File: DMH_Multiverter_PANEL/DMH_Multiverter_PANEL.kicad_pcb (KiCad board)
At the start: 2 copper layers, 50 x 200 mm, 5 parts, among them J0 Panel_GND_Solder_Wire_Pad

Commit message: Panel ready
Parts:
- added H10: Attenuate, SynthStuff:Pot_Cutout_Small_attv, F.Cu at (83.0, 97.0)
- added H11: Input, SynthStuff:Jack_6.35mm_Cutout_v3, F.Cu at (58.5, 126.2)
- added H12: Output, SynthStuff:Jack_6.35mm_Cutout_Output_v6, F.Cu at (75.0, 126.2)
- added H13: Output, SynthStuff:Jack_6.35mm_Cutout_Output_v6, F.Cu at (91.5, 126.2)
- added H14: Input, SynthStuff:Jack_6.35mm_Cutout_v3, F.Cu at (58.5, 142.8)
- added H15: Output, SynthStuff:Jack_6.35mm_Cutout_Output_v6, F.Cu at (75.0, 142.8)
- added H16: Output, SynthStuff:Jack_6.35mm_Cutout_Output_v6, F.Cu at (91.5, 142.8)
- added H17: Input, SynthStuff:Jack_6.35mm_Cutout_v3, F.Cu at (58.5, 159.2)
- added H18: Output, SynthStuff:Jack_6.35mm_Cutout_Output_v6, F.Cu at (75.0, 159.2)
- added H19: Output, SynthStuff:Jack_6.35mm_Cutout_Output_v6, F.Cu at (91.5, 159.2)
- added H20: Input, SynthStuff:Jack_6.35mm_Cutout_v3, F.Cu at (58.5, 175.8)
- added H21: Output, SynthStuff:Jack_6.35mm_Cutout_Output_v6, F.Cu at (75.0, 175.8)
- added H22: Output, SynthStuff:Jack_6.35mm_Cutout_Output_v6, F.Cu at (91.5, 175.8)
- added H23: Input, SynthStuff:Jack_6.35mm_Cutout_v3, F.Cu at (58.5, 192.2)
- added H24: Output, SynthStuff:Jack_6.35mm_Cutout_Output_v6, F.Cu at (75.0, 192.2)
- added H25: Output, SynthStuff:Jack_6.35mm_Cutout_Output_v6, F.Cu at (91.5, 192.2)
- added H26: Input, SynthStuff:Jack_6.35mm_Cutout_v3, F.Cu at (58.5, 208.8)
- added H27: Output, SynthStuff:Jack_6.35mm_Cutout_Output_v6, F.Cu at (75.0, 208.8)
- added H28: Output, SynthStuff:Jack_6.35mm_Cutout_Output_v6, F.Cu at (91.5, 208.8)
- added H5: Input, SynthStuff:Jack_6.35mm_Cutout_v3, F.Cu at (58.5, 50.0)
- added H6: Output, SynthStuff:Jack_6.35mm_Cutout_Output_v6, F.Cu at (58.5, 67.0)
- added H7: Attenuate, SynthStuff:Pot_Cutout_Small_attv, F.Cu at (83.0, 58.8)
- added H8: Input, SynthStuff:Jack_6.35mm_Cutout_v3, F.Cu at (58.5, 88.2)
- added H9: Output, SynthStuff:Jack_6.35mm_Cutout_Output_v6, F.Cu at (58.5, 105.2)
- moved J0 65.6 mm to (95.0, 78.0)
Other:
- board text added: "Attn & Mult"
- board text removed: "Module Name"
- board text removed: "TYPE"

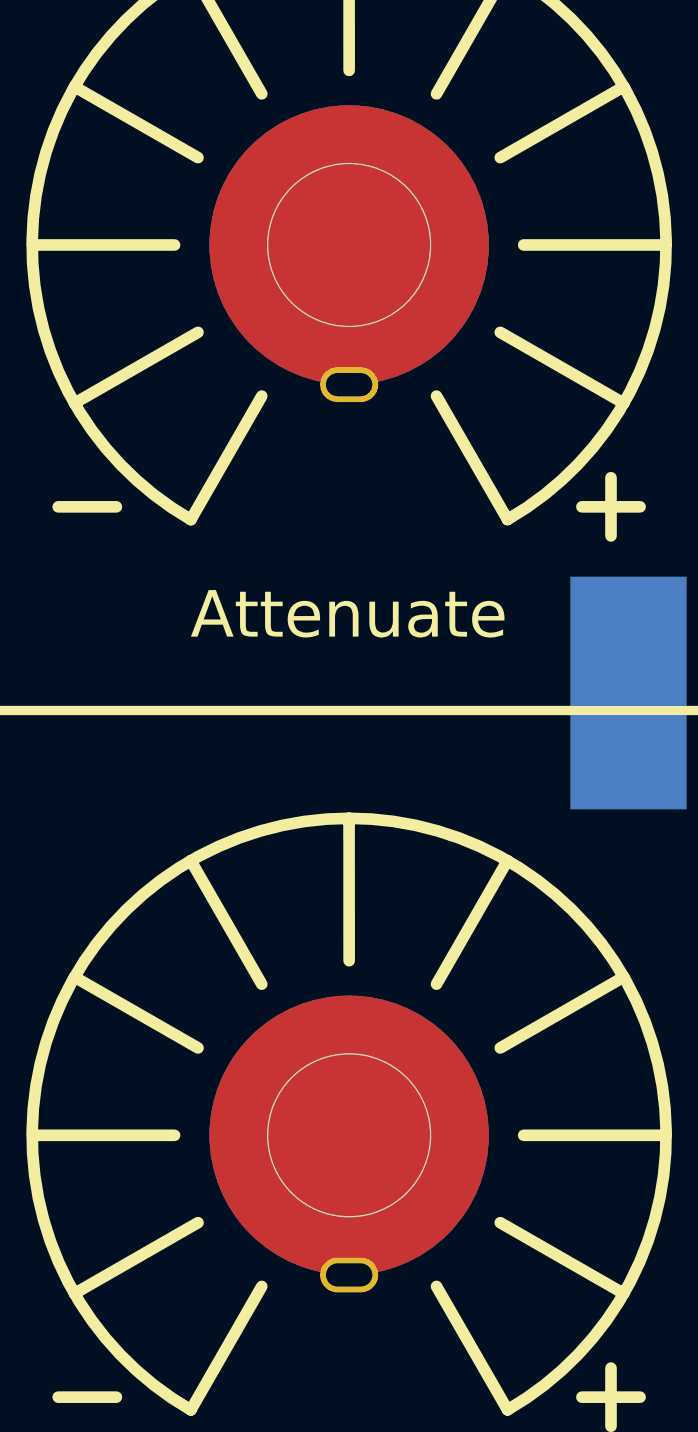
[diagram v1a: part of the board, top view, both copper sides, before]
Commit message: Adapted design to center detent pot P110KH-1F15
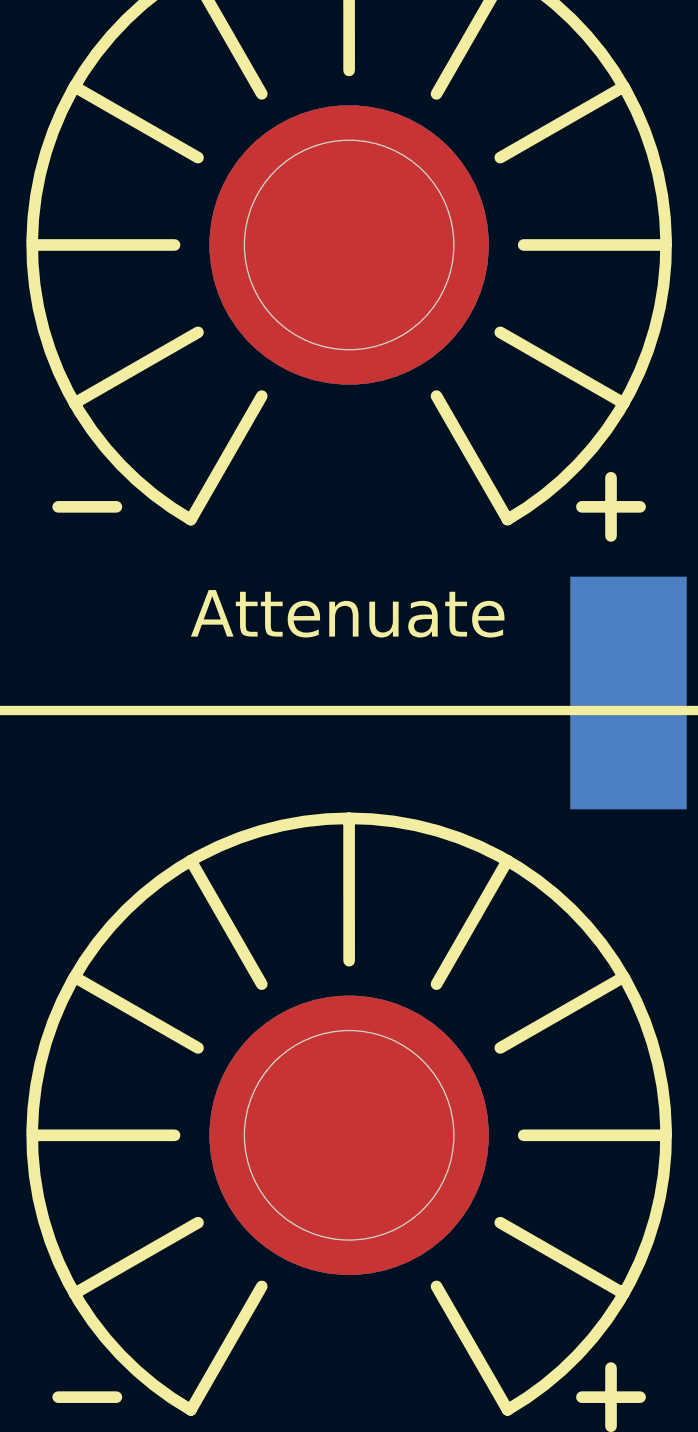
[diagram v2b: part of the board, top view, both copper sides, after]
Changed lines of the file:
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@@
 		(fp_circle
 			(center 0 0)
-			(end 0 3.5)
+			(end 4.5 0)
 			(stroke
 				(width 0.05)
@@
 			(size 12 12)
 			(layers "B.Cu" "B.Mask")
-			(net 1 "GND")
-			(pinfunction "1")
-			(pintype "input")
-			(zone_connect 2)
-		)
-		(pad "1" thru_hole oval
-			(at 0 6)
-			(size 2.5 1.5)
-			(drill oval 2 1)
-			(layers "*.Cu" "*.Mask")
-			(remove_unused_layers no)
 			(net 1 "GND")
 			(pinfunction "1")
@@
 		(fp_circle
 			(center 0 0)
-			(end 0 3.5)
+			(end 4.5 0)
 			(stroke
 				(width 0.05)
@@
 			(net 1 "GND")
 			(pinfunction "1")
-			(pintype "input")
-			(zone_connect 2)
-		)
-		(pad "1" thru_hole oval
-			(at 0 6)
-			(size 2.5 1.5)
-			(drill oval 2 1)
-			(layers "*.Cu" "*.Mask")
-			(remove_unused_layers no)
-			(net 1 "GND")
-			(pinfunction "1")

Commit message: Created Gerbers
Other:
- board text added: "Mk1.0 - December 2024"
- board text removed: "Mk1.0 - Month Year"
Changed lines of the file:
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@@
 			(plot_on_all_layers_selection 0x0000000_00000000)
 			(disableapertmacros no)
-			(usegerberextensions no)
+			(usegerberextensions yes)
 			(usegerberattributes yes)
 			(usegerberadvancedattributes yes)
@@
 			(plotinvisibletext no)
 			(sketchpadsonfab no)
-			(subtractmaskfromsilk no)
+			(subtractmaskfromsilk yes)
 			(outputformat 1)
 			(mirror no)
-			(drillshape 1)
+			(drillshape 0)
 			(scaleselection 1)
-			(outputdirectory "")
+			(outputdirectory "Gerbers/")
 		)
 	)
@@
 		(layer "F.Cu")
 		(at 83 97)
+		(descr "Based on TT P110KH1-1F15BR100K")
 		(property "Reference" "H10"
 			(at 0 -7.9 0)
@@
 		(layer "F.Cu")
 		(at 83 58.75)
+		(descr "Based on TT P110KH1-1F15BR100K")
 		(property "Reference" "H7"
 			(at 0 -7.9 0)
@@
 		(layer "User.9")
 	)
-	(gr_text "Mk1.0 - Month Year"
+	(gr_text "Mk1.0 - December 2024"
 		(at 75 222.95 0)
 		(layer "B.SilkS")

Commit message: Sync libs
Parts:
- H10, H7: footprint SynthStuff:Pot_Cutout_Small_attv -> SynthStuff:Pot_Cutout_Small_attv_P110KH1
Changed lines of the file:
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@@
 		)
 	)
-	(footprint "SynthStuff:Pot_Cutout_Small_attv"
+	(footprint "SynthStuff:Pot_Cutout_Small_attv_P110KH1"
 		(layer "F.Cu")
 		(at 83 97)
@@
 			)
 		)
-		(property "Footprint" "SynthStuff:Pot_Cutout_Small_attv"
+		(property "Footprint" "SynthStuff:Pot_Cutout_Small_attv_P110KH1"
 			(at 0 0 0)
 			(unlocked yes)
@@
 		(sheetname "Root")
 		(sheetfile "DMH_Multiverter_PANEL.kicad_sch")
-		(attr through_hole exclude_from_bom)
+		(attr through_hole)
 		(fp_line
 			(start -12.5 11.25)
@@
 		)
 	)
-	(footprint "SynthStuff:Pot_Cutout_Small_attv"
+	(footprint "SynthStuff:Pot_Cutout_Small_attv_P110KH1"
 		(layer "F.Cu")
 		(at 83 58.75)
@@
 			)
 		)
-		(property "Footprint" "SynthStuff:Pot_Cutout_Small_attv"
+		(property "Footprint" "SynthStuff:Pot_Cutout_Small_attv_P110KH1"
 			(at 0 0 0)
 			(unlocked yes)
@@
 		(sheetname "Root")
 		(sheetfile "DMH_Multiverter_PANEL.kicad_sch")
-		(attr through_hole exclude_from_bom)
+		(attr through_hole)
 		(fp_line
 			(start -12.5 11.25)
